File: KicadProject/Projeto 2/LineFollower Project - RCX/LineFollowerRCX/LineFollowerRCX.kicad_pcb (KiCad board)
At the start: 2 copper layers, 100 x 70.9 mm, 13 parts, among them J1 Conn_01x11_Pin, J10 GND pinos, J2 Motor 1, J3 Motor 1, J4 Modulo bluetooth, J7 Conector sensor lateral Esque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, J8 Conector sensor lateral Direi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, J9 VCC pinos, U1 ROB-14450, U2 LM7805_TO220

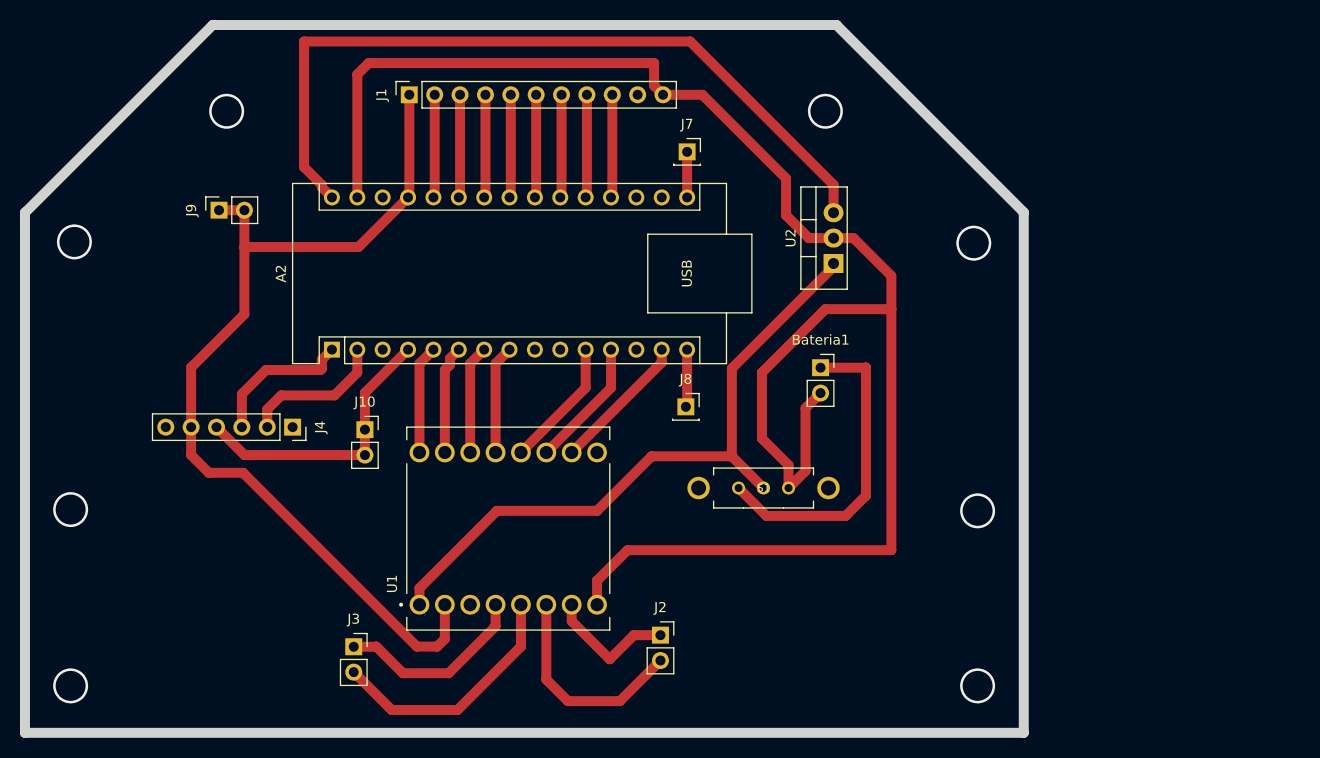
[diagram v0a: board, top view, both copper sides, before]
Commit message: Codigos de teste e pcb invertida
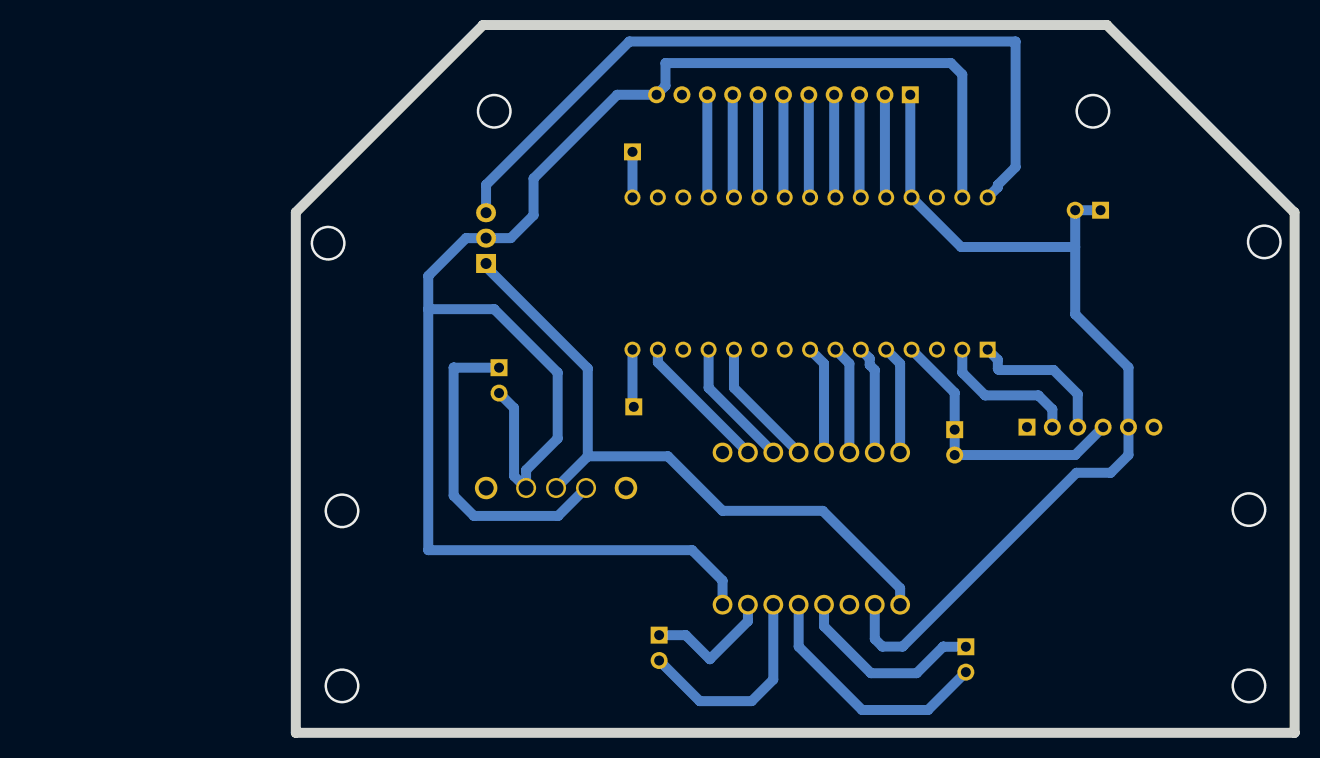
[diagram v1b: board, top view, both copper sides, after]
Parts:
- A2, Bateria1, J1, J10, J2, J3, J4, J7, J8, J9, S1, U1, U2: moved to B.Cu
- moved J9 88.3 mm to (219.1, 102.7)
- moved J4 73.5 mm to (211.7, 124.5)
- moved A2 65.7 mm to (207.8, 116.7)
- moved J3 61.3 mm to (205.6, 146.5), turned to 180 degrees
- moved J10 59.0 mm to (204.5, 124.7), turned to 180 degrees
- moved J1 50.2 mm to (200.0, 91.2)
- moved U2 34.8 mm to (157.5, 108.1)
- moved Bateria1 32.2 mm to (158.8, 118.5), turned to 180 degrees
- moved U1 30.3 mm to (190.1, 134.6)
- moved S1 20.8 mm to (164.6, 130.6), turned to 180 degrees
- moved J7 5.47 mm to (172.2, 96.9), turned to 180 degrees
- moved J8 5.22 mm to (172.3, 122.4), turned to 180 degrees
- moved J2 0.14 mm to (174.9, 145.3), turned to 180 degrees
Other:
- outline, holes or cut-outs redrawn
